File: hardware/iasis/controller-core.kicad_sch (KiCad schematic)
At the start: 39 parts, among them J1101 TSW-104-07-G-D, SW1101 PTS645SL50SMTR92LFS, SW1102 PTS645SL50SMTR92LFS, U1101 RP2354B, Y1101 ABM8-272-T3

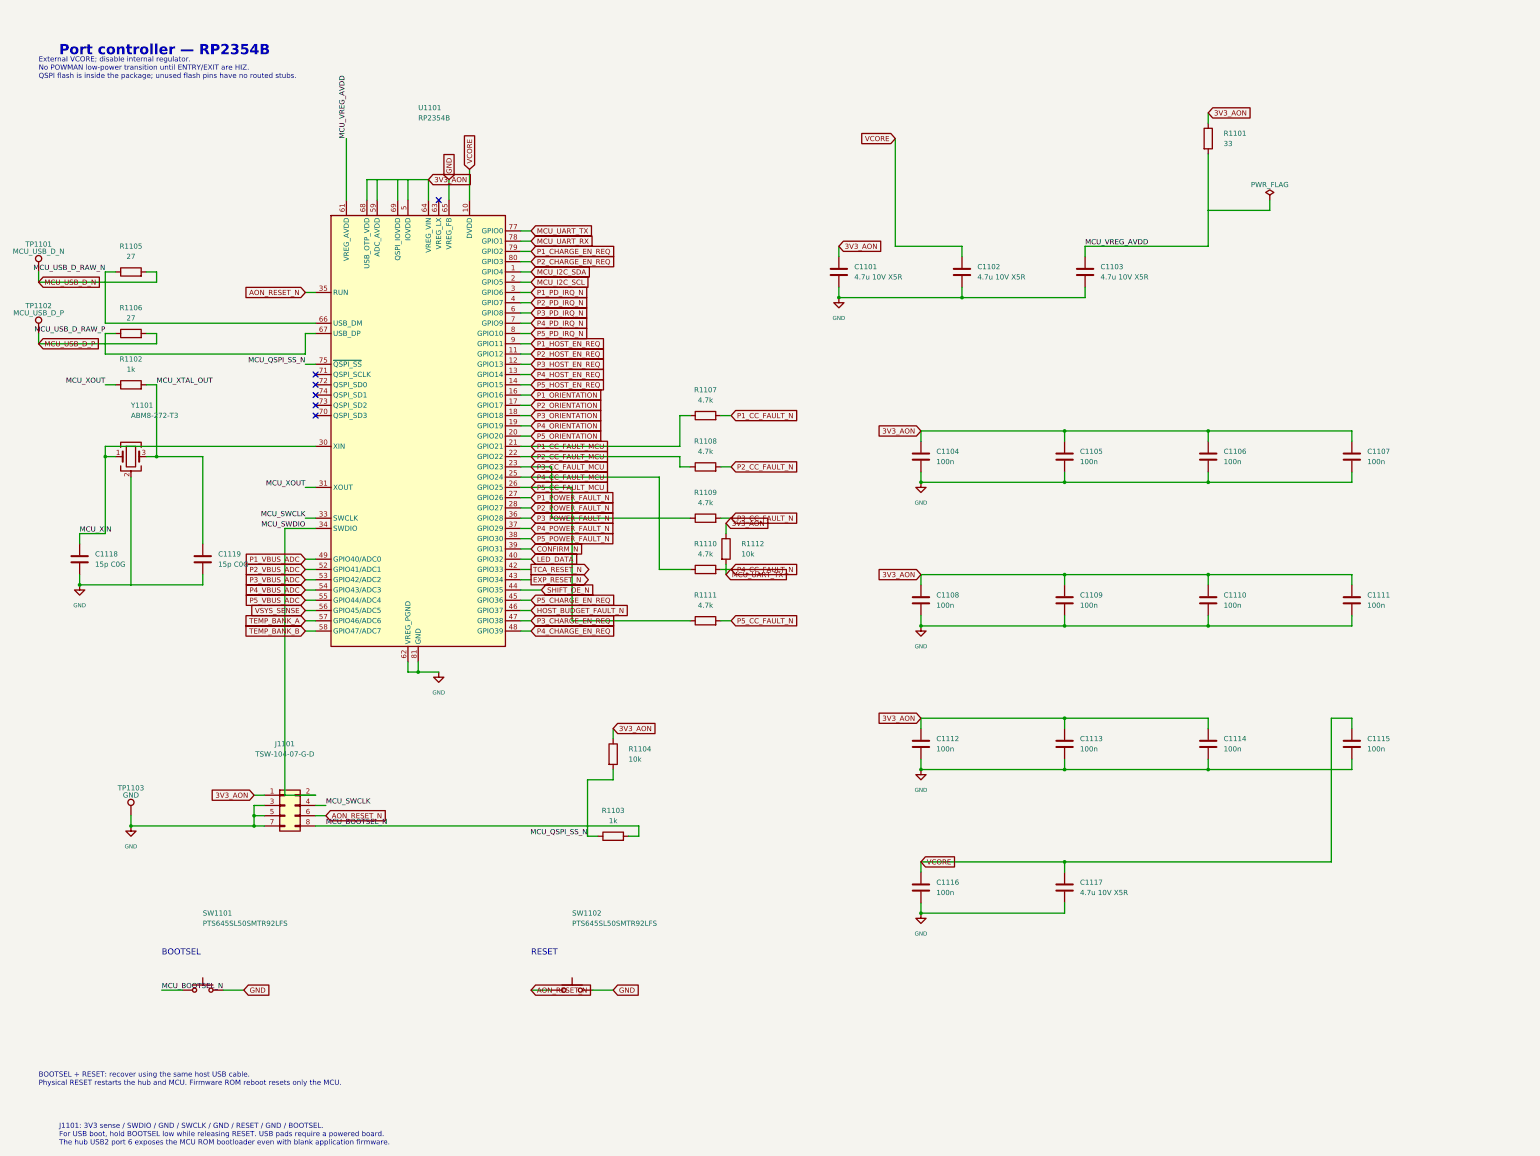
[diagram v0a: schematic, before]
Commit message: Wire the schematic islands and side-match the RP2354 GPIOs
Each sheet now draws its circuits with wires. Labels remain at block edges
and on single-part islands: buttons, test points, decoupling and pull
resistors. The target-port page wires its hierarchical labels straight to
the child sheet pins, the ports page points its labels away from each
block, and the root sheet keeps every block clear of the title block.

The RP2354B GPIOs are reassigned so each signal leaves the package on the
side facing its destination. Update PCB from Schematic applied the 43
U1101 pad-net changes with no geometry change. Otherwise the netlist
matches the previous design, ERC keeps its 14 existing warnings and DRC
reports no parity issues.
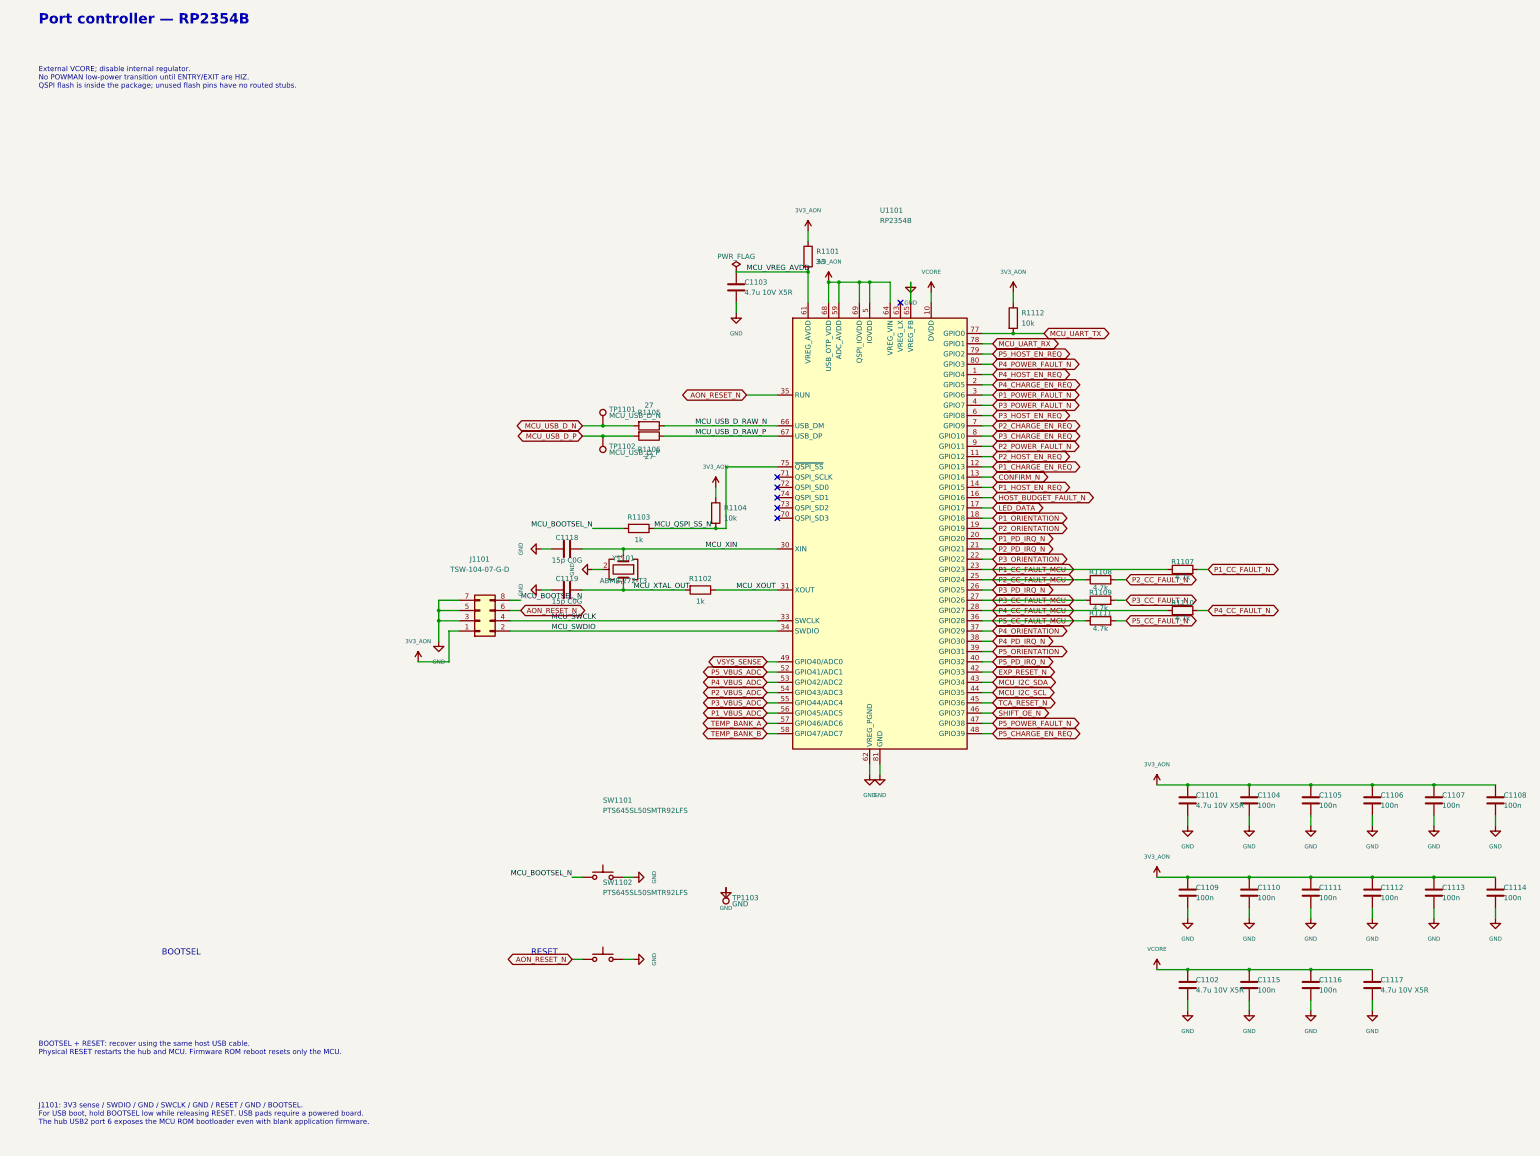
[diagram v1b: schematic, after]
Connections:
- net CONFIRM_N: now also U1101.13 (GPIO14); no longer U1101.39 (GPIO31)
- net EXP_RESET_N: now also U1101.42 (GPIO33); no longer U1101.43 (GPIO34)
- net HOST_BUDGET_FAULT_N: now also U1101.16 (GPIO16); no longer U1101.46 (GPIO37)
- net LED_DATA: now also U1101.17 (GPIO17); no longer U1101.40 (GPIO32)
- net MCU_I2C_SCL: now also U1101.44 (GPIO35); no longer U1101.2 (GPIO5)
- net MCU_I2C_SDA: now also U1101.43 (GPIO34); no longer U1101.1 (GPIO4)
- net P1_CC_FAULT_MCU: now also U1101.23 (GPIO23); no longer U1101.21 (GPIO21)
- net P1_CHARGE_EN_REQ: now also U1101.12 (GPIO13); no longer U1101.79 (GPIO2)
- net P1_HOST_EN_REQ: now also U1101.14 (GPIO15); no longer U1101.9 (GPIO11)
- net P1_ORIENTATION: now also U1101.18 (GPIO18); no longer U1101.16 (GPIO16)
- net P1_PD_IRQ_N: now also U1101.20 (GPIO20); no longer U1101.3 (GPIO6)
- net P1_POWER_FAULT_N: now also U1101.3 (GPIO6); no longer U1101.27 (GPIO26)
- net P1_VBUS_ADC: now also U1101.56 (GPIO45/ADC5); no longer U1101.49 (GPIO40/ADC0)
- net P2_CC_FAULT_MCU: now also U1101.25 (GPIO24); no longer U1101.22 (GPIO22)
- net P2_CHARGE_EN_REQ: now also U1101.7 (GPIO9); no longer U1101.80 (GPIO3)
- net P2_ORIENTATION: now also U1101.19 (GPIO19); no longer U1101.17 (GPIO17)
- net P2_PD_IRQ_N: now also U1101.21 (GPIO21); no longer U1101.4 (GPIO7)
- net P2_POWER_FAULT_N: now also U1101.9 (GPIO11); no longer U1101.28 (GPIO27)
- net P2_VBUS_ADC: now also U1101.54 (GPIO43/ADC3); no longer U1101.52 (GPIO41/ADC1)
- net P3_CC_FAULT_MCU: now also U1101.27 (GPIO26); no longer U1101.23 (GPIO23)
- net P3_CHARGE_EN_REQ: now also U1101.8 (GPIO10); no longer U1101.47 (GPIO38)
- net P3_HOST_EN_REQ: now also U1101.6 (GPIO8); no longer U1101.12 (GPIO13)
- net P3_ORIENTATION: now also U1101.22 (GPIO22); no longer U1101.18 (GPIO18)
- net P3_PD_IRQ_N: now also U1101.26 (GPIO25); no longer U1101.6 (GPIO8)
- net P3_POWER_FAULT_N: now also U1101.4 (GPIO7); no longer U1101.36 (GPIO28)
- net P3_VBUS_ADC: now also U1101.55 (GPIO44/ADC4); no longer U1101.53 (GPIO42/ADC2)
- net P4_CC_FAULT_MCU: now also U1101.28 (GPIO27); no longer U1101.25 (GPIO24)
- net P4_CHARGE_EN_REQ: now also U1101.2 (GPIO5); no longer U1101.48 (GPIO39)
- net P4_HOST_EN_REQ: now also U1101.1 (GPIO4); no longer U1101.13 (GPIO14)
- net P4_ORIENTATION: now also U1101.37 (GPIO29); no longer U1101.19 (GPIO19)
- net P4_PD_IRQ_N: now also U1101.38 (GPIO30); no longer U1101.7 (GPIO9)
- net P4_POWER_FAULT_N: now also U1101.80 (GPIO3); no longer U1101.37 (GPIO29)
- net P4_VBUS_ADC: now also U1101.53 (GPIO42/ADC2); no longer U1101.54 (GPIO43/ADC3)
- net P5_CC_FAULT_MCU: now also U1101.36 (GPIO28); no longer U1101.26 (GPIO25)
- net P5_CHARGE_EN_REQ: now also U1101.48 (GPIO39); no longer U1101.45 (GPIO36)
- net P5_HOST_EN_REQ: now also U1101.79 (GPIO2); no longer U1101.14 (GPIO15)
- net P5_ORIENTATION: now also U1101.39 (GPIO31); no longer U1101.20 (GPIO20)
- net P5_PD_IRQ_N: now also U1101.40 (GPIO32); no longer U1101.8 (GPIO10)
- net P5_POWER_FAULT_N: now also U1101.47 (GPIO38); no longer U1101.38 (GPIO30)
- net P5_VBUS_ADC: now also U1101.52 (GPIO41/ADC1); no longer U1101.55 (GPIO44/ADC4)
- net SHIFT_OE_N: now also U1101.46 (GPIO37); no longer U1101.44 (GPIO35)
- net TCA_RESET_N: now also U1101.45 (GPIO36); no longer U1101.42 (GPIO33)
- net VSYS_SENSE: now also U1101.49 (GPIO40/ADC0); no longer U1101.56 (GPIO45/ADC5)
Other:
- moved on the sheet: C1101, C1102, C1103, C1104, C1105, C1106, C1107, C1108, C1109, C1110, C1111, C1112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

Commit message: Redraw the RP2354 controller sheet
Supplies tie to two rails above the chip with their decoupling, the
crystal and load capacitors sit under XIN and XOUT, and the SWD header
wires straight to the RESET and BOOTSEL buttons. GPIO labels stay on
the right with the CC-fault series resistors beside them. The netlist
is unchanged.
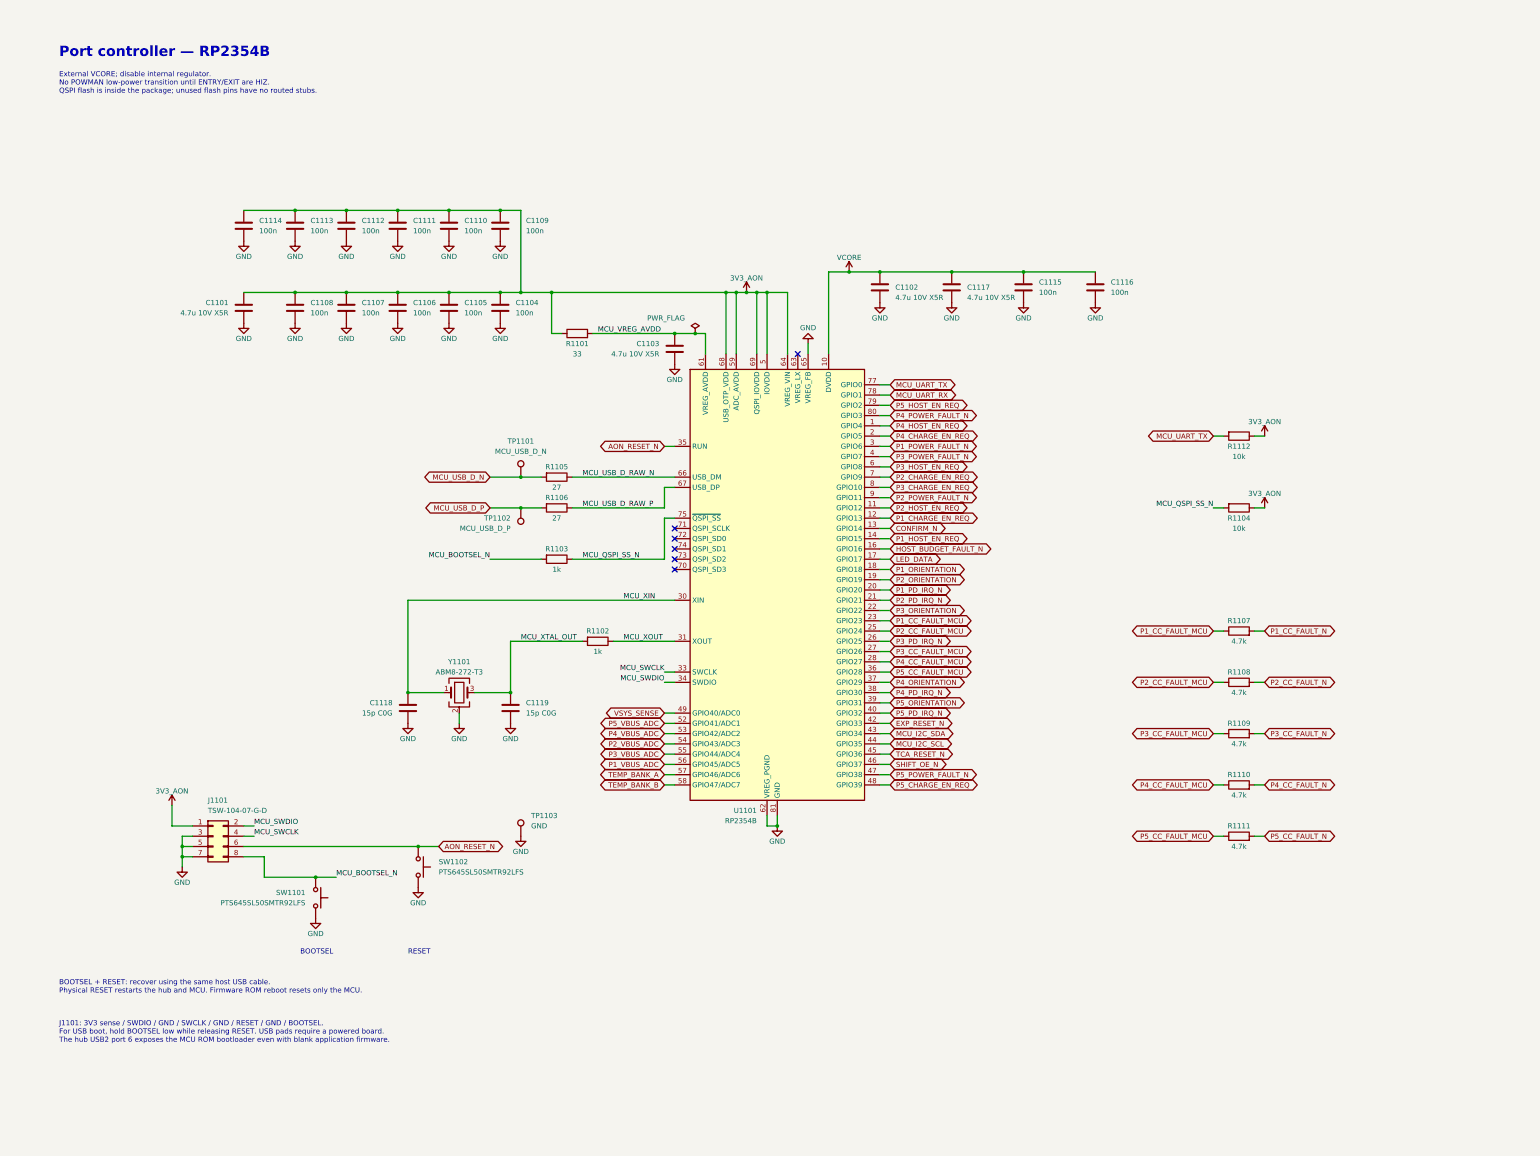
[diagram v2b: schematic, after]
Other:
- title: (none) -> Port controller — RP2354B
- moved on the sheet: C1101, C1102, C1103, C1104, C1105, C1106, C1107, C1108, C1109, C1110, C1111, C1112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
